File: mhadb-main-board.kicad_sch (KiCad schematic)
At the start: 113 parts, among them J1 Conn_01x04, J10 Conn_01x04_Pin, J2 Conn_01x04, J3 USB_C_Receptacle_USB2.0_14P, J4 Conn_01x02, J5 Conn_01x03, J6 Conn_01x03, J7 Conn_01x04, J8 Conn_01x04, J9 Conn_01x04_Pin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

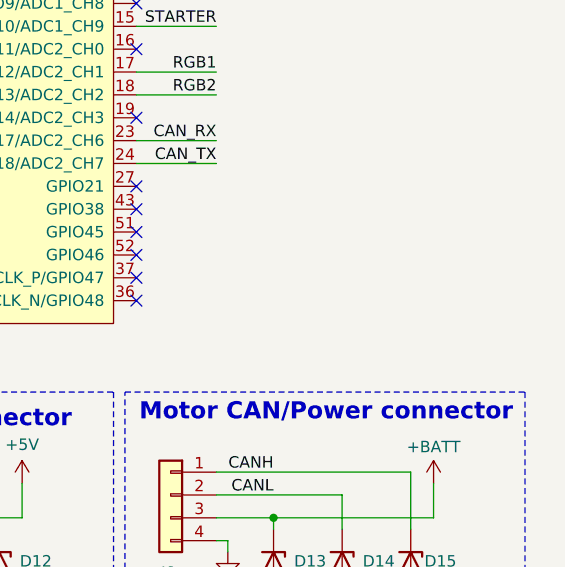
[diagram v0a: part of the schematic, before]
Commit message: schem/pcb: add mounting holes
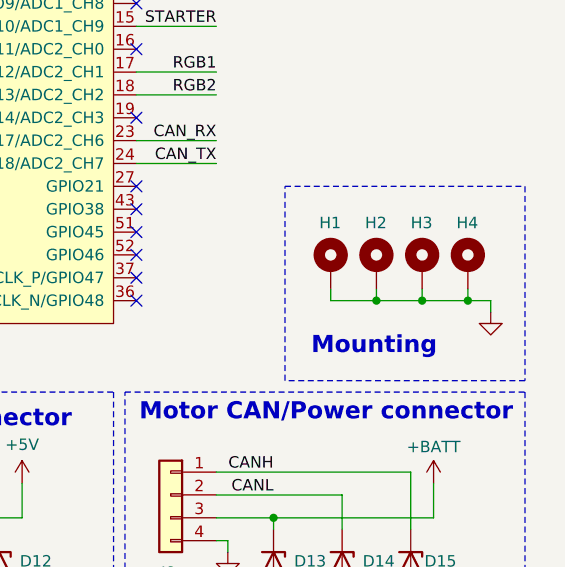
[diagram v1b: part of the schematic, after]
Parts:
- added H1, H2, H3, H4: MountingHole_Pad, GLCS:MountingHole_3.2mm_M3_DIN965_Pad_Thin, symbol Mechanical:MountingHole_Pad
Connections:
- net GND: now also H1.1, H2.1, H3.1, H4.1
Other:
- note added: "Mounting"

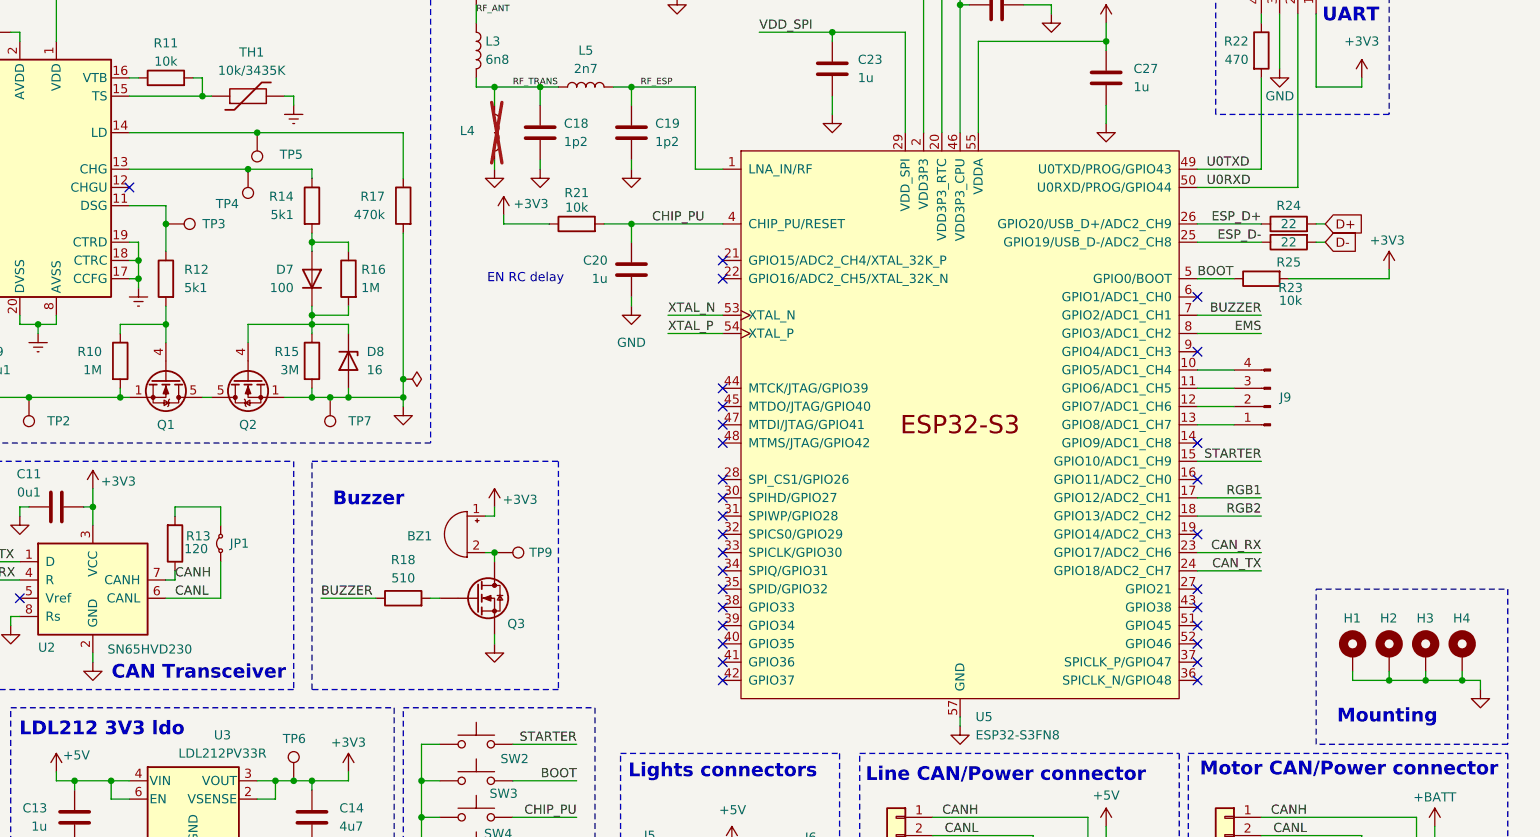
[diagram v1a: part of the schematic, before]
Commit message: schem: remove extra testpoints
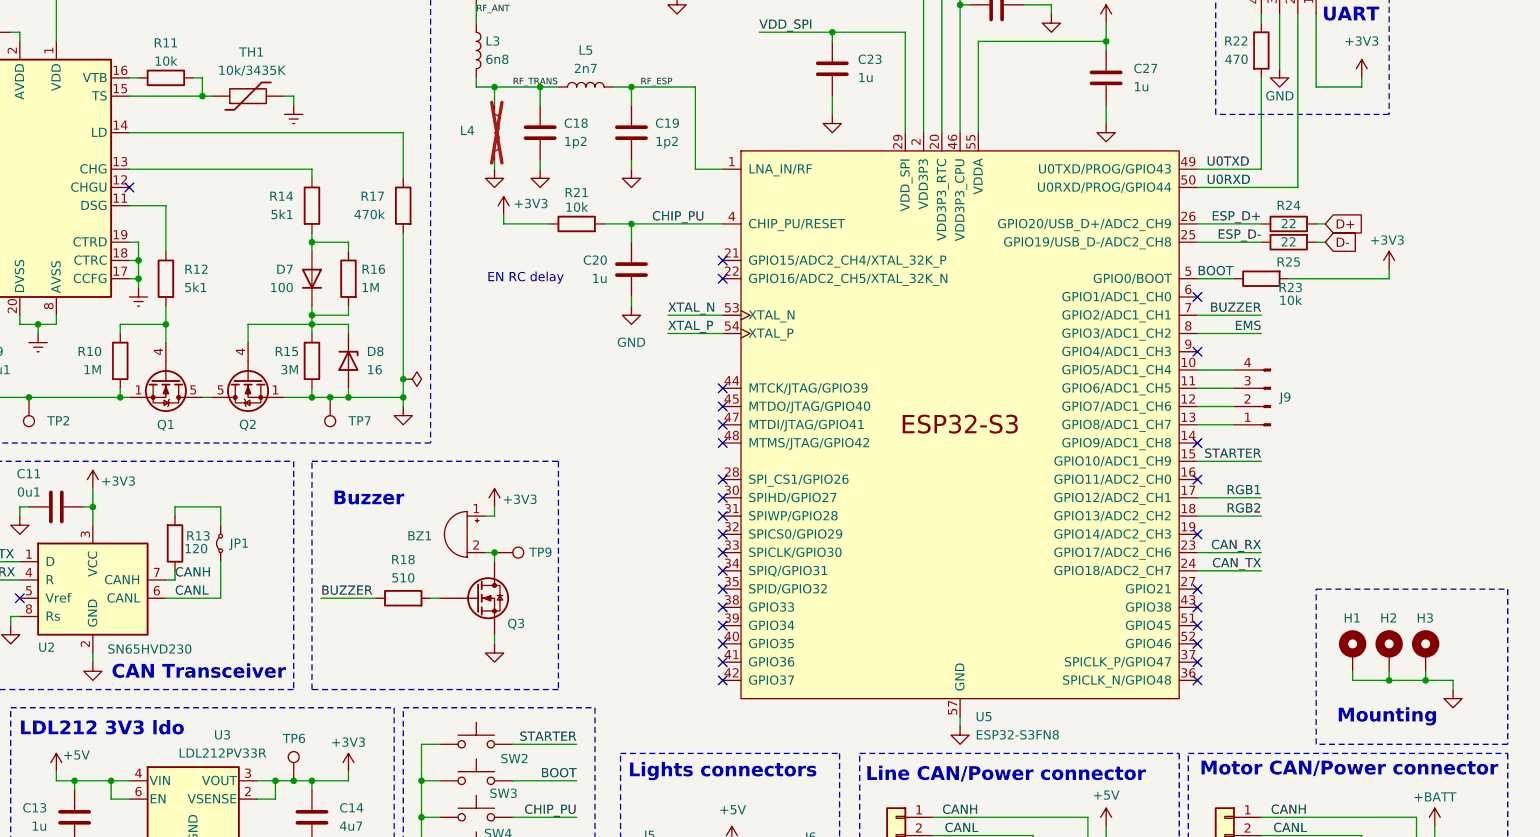
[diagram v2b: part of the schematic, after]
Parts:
- removed H3: MountingHole_Pad, GLCS:MountingHole_3.2mm_M3_DIN965_Pad_Thin, symbol Mechanical:MountingHole_Pad
- removed TP3, TP4, TP5: TestPoint, TestPoint:TestPoint_Pad_D2.0mm, symbol Connector:TestPoint
- renumbered H4 to H3
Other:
- moved on the sheet: H3

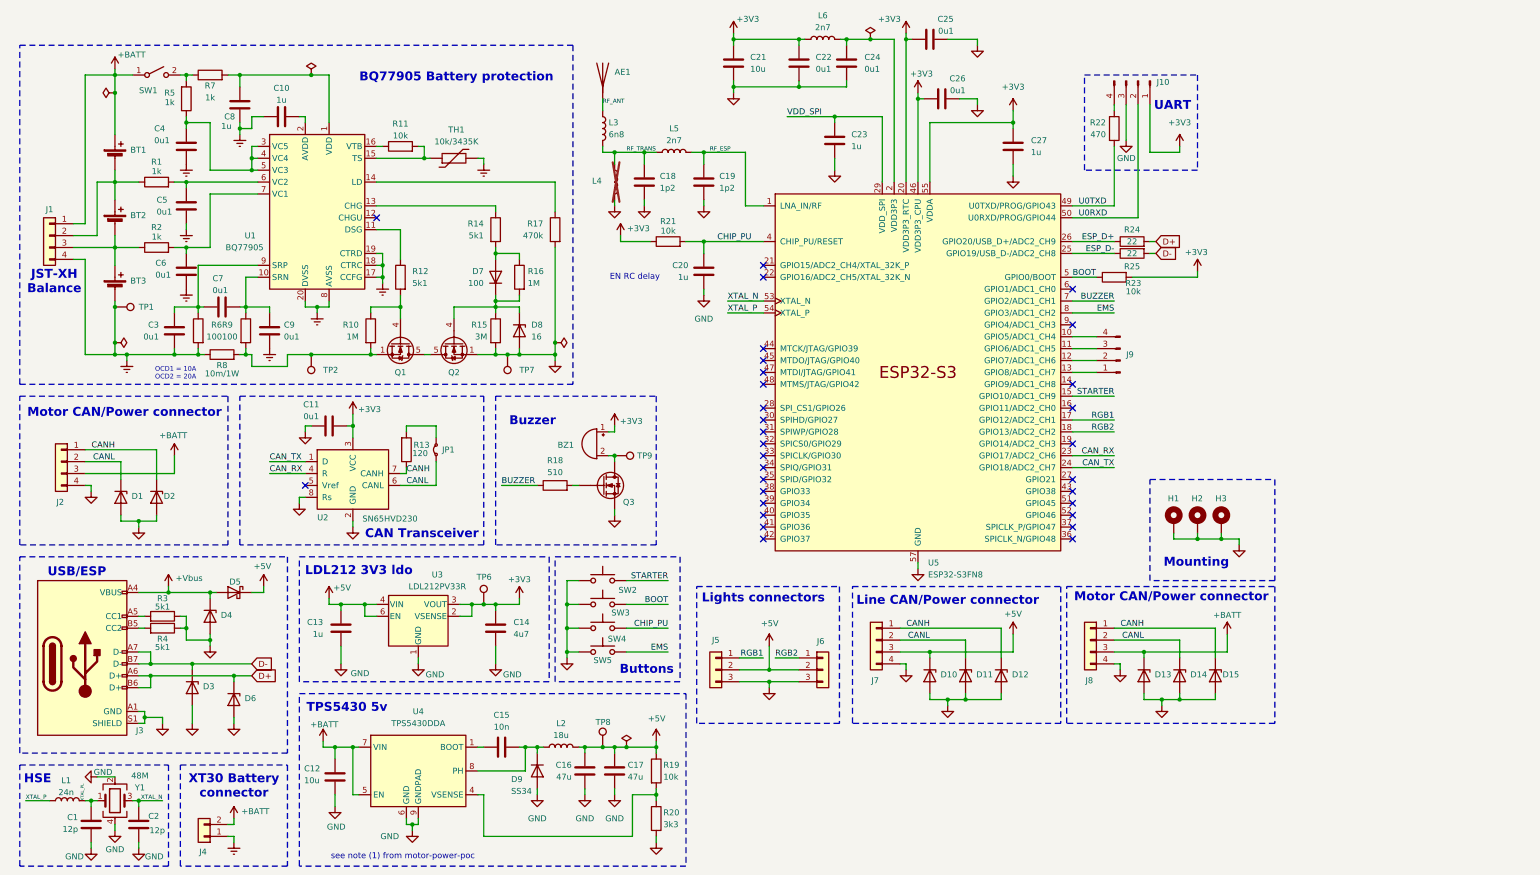
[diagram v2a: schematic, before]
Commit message: pcb: initial layout
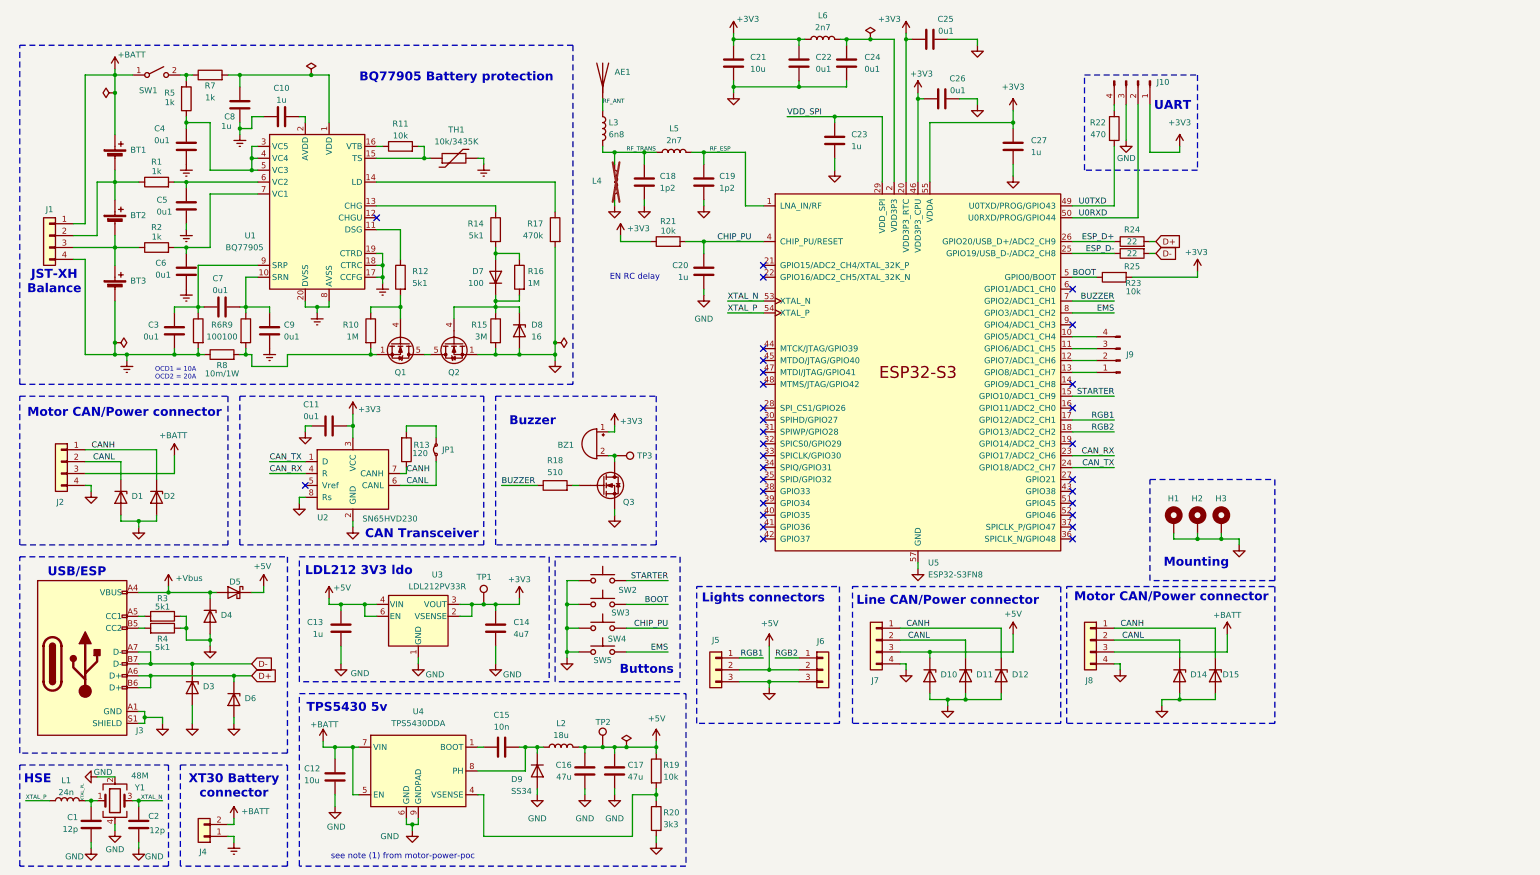
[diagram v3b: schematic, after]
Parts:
- removed D13: H5VU10U, GLCS:Diode_DFN1006, symbol GLCS:H5VU10U
- removed TP1, TP2, TP7: TestPoint, TestPoint:TestPoint_Pad_D2.0mm, symbol Connector:TestPoint
- renumbered TP6 to TP1, TP8 to TP2, TP9 to TP3

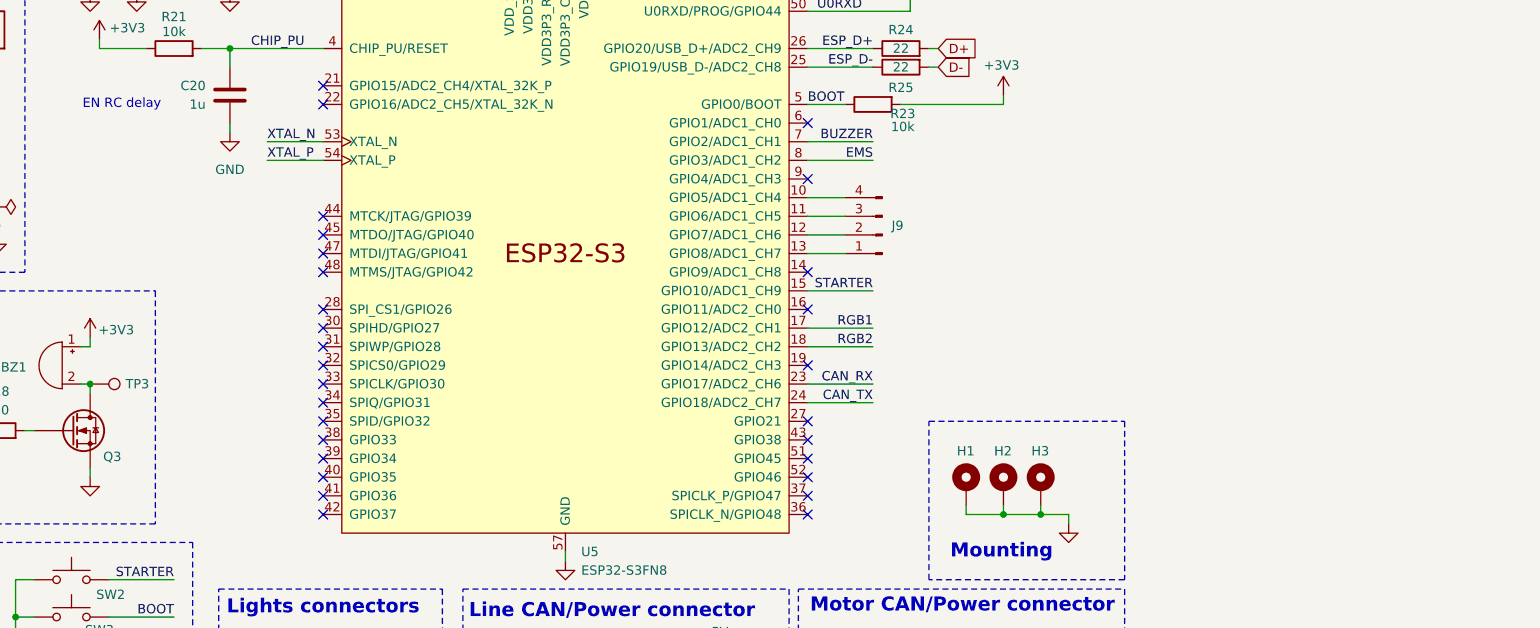
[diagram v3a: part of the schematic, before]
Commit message: schem/pcb: add TMP117 temp sensor
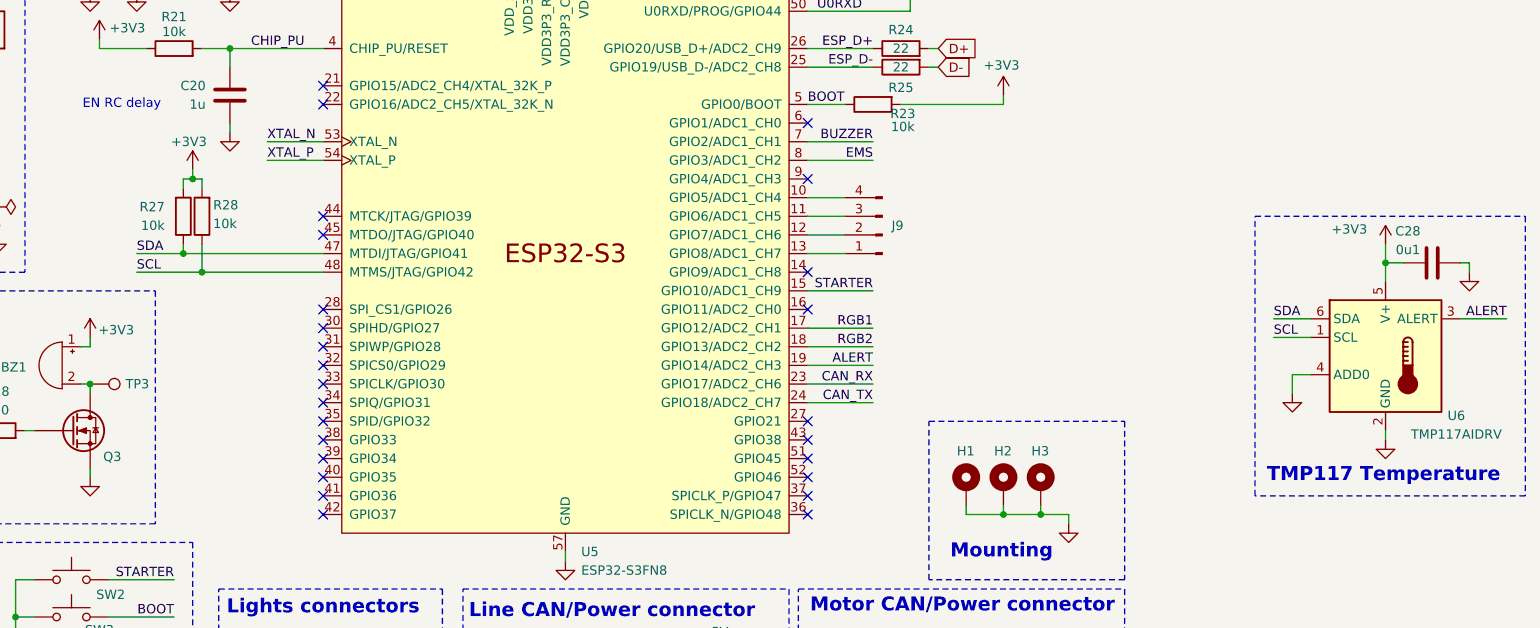
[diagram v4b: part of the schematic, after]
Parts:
- added C28: 0u1, Capacitor_SMD:C_0402_1005Metric, symbol Device:C
- added R27, R28: 10k, Resistor_SMD:R_0402_1005Metric, symbol Device:R
- added U6: TMP117AIDRV, Package_SON:WSON-6-1EP_2x2mm_P0.65mm_EP1x1.6mm, symbol Sensor_Temperature:TMP117xxDRV
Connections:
- net +3V3: now also C28.1, R27.2, R28.2, U6.5 (V+)
- net GND: now also C28.2, U6.2 (GND), U6.4 (ADD0)
- net ALERT: now reaches U5.19 (GPIO14/ADC2_CH3)
- net ALERT: now also U6.3 (ALERT)
- net SDA: now reaches U5.47 (MTDI/JTAG/GPIO41)
- net SDA: now also R27.1, U6.6 (SDA)
- net SCL: now reaches U5.48 (MTMS/JTAG/GPIO42)
- net SCL: now also R28.1, U6.1 (SCL)
- no-connect marks 31 -> 28
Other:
- note added: "TMP117 Temperature"
